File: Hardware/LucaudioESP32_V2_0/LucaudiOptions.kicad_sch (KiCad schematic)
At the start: 17 parts, among them J1 Conn_01x04_Pin, J6 Conn_01x05_Pin, Q1 BC847, Q2 BC847, SW3 RotaryEncoder_Switch

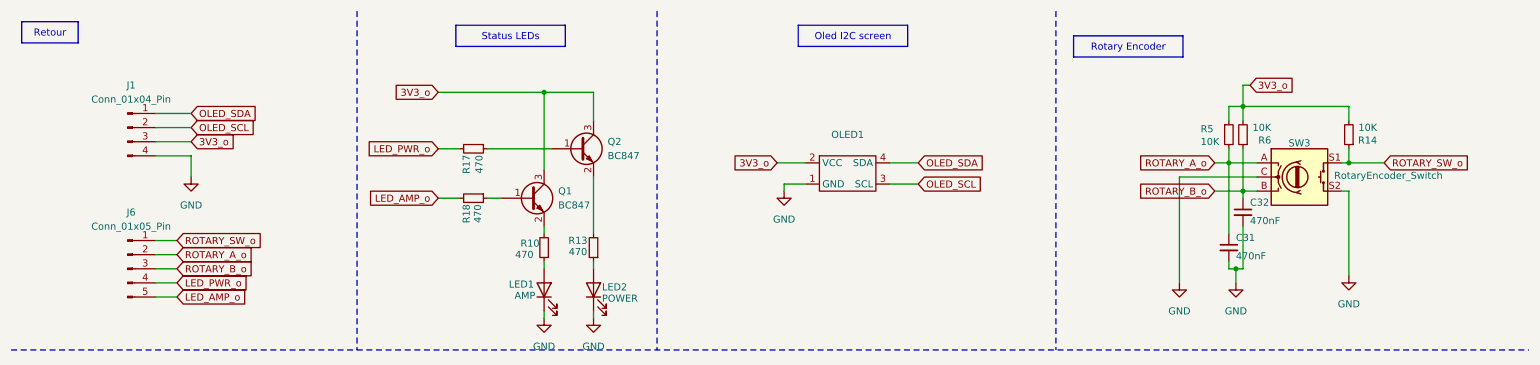
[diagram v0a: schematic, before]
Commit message: Revamping folders and added 2.0 and 2.1 on git
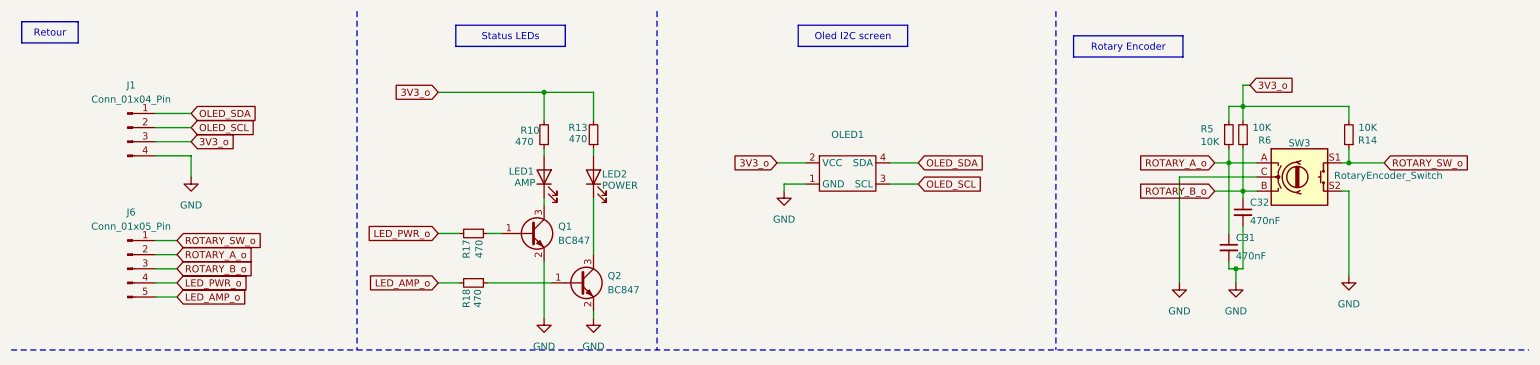
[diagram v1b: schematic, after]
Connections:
- net 3V3_o: now also R10.2, R13.2; no longer Q1.3 (C), Q2.3 (C)
- net GND: now also Q1.2 (E), Q2.2 (E); no longer LED1.1 (K), LED2.1 (K)
- net at R17.1: now also Q1.1 (B); no longer Q2.1 (B)
- net at R18.1: now also Q2.1 (B); no longer Q1.1 (B)
- new net: LED1.1 (K), Q1.3 (C)
- new net: LED2.1 (K), Q2.3 (C)
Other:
- moved on the sheet: LED1, LED2, R10, R13, R17, R18
